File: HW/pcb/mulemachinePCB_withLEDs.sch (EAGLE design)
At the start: 29 parts, among them IC1 LD117AV50, IC2 MEGA8-P, J1 DCJ0202, Q1 16Mhz

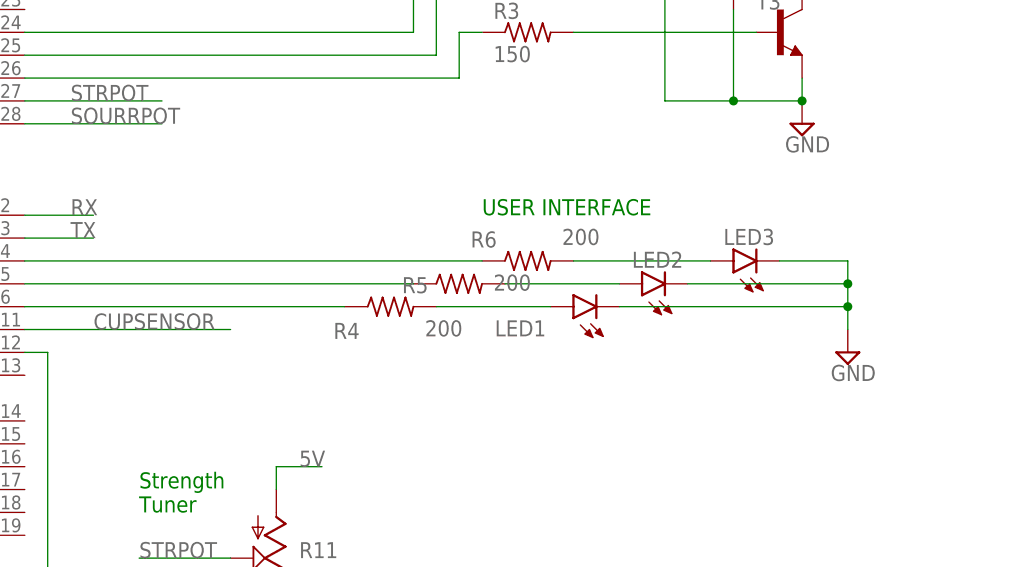
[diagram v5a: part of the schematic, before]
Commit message: preparing files for first prototype of version 1.0 of Mule Machine. Corrected Code to reflect Orange and Green LEDs being flipped on PCB and Code. Used PCB Version. Added some new design features to laser panel and PCB for version 1.1
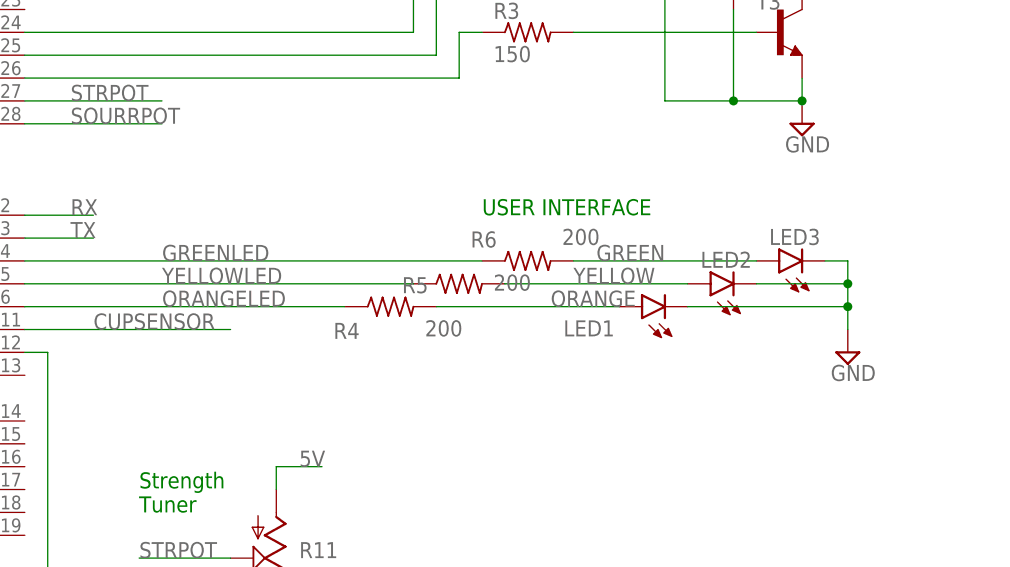
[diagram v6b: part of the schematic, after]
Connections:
- net N$2 renamed ORANGELED
- net N$25 renamed ORANGE
- net N$26 renamed YELLOW
- net N$27 renamed GREEN
- net N$3 renamed YELLOWLED
- net N$4 renamed GREENLED
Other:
- moved on the sheet: LED1, LED2, LED3
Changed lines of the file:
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@@
 <grid distance="0.1" unitdist="inch" unit="inch" style="lines" multiple="1" display="no" altdistance="0.01" altunitdist="inch" altunit="inch"/>
 <layers>
-<layer number="1" name="Top" color="4" fill="1" visible="yes" active="no"/>
-<layer number="16" name="Bottom" color="1" fill="1" visible="yes" active="no"/>
-<layer number="17" name="Pads" color="2" fill="1" visible="yes" active="no"/>
-<layer number="18" name="Vias" color="2" fill="1" visible="yes" active="no"/>
-<layer number="19" name="Unrouted" color="6" fill="1" visible="yes" active="no"/>
-<layer number="20" name="Dimension" color="24" fill="1" visible="yes" active="no"/>
-<layer number="21" name="tPlace" color="7" fill="1" visible="yes" active="no"/>
-<layer number="22" name="bPlace" color="7" fill="1" visible="yes" active="no"/>
-<layer number="23" name="tOrigins" color="15" fill="1" visible="yes" active="no"/>
-<layer number="24" name="bOrigins" color="15" fill="1" visible="yes" active="no"/>
-<layer number="25" name="tNames" color="7" fill="1" visible="yes" active="no"/>
-<layer number="26" name="bNames" color="7" fill="1" visible="yes" active="no"/>
-<layer number="27" name="tValues" color="7" fill="1" visible="yes" active="no"/>
-<layer number="28" name="bValues" color="7" fill="1" visible="yes" active="no"/>
+<layer number="1" name="Top" color="4" fill="1" visible="no" active="no"/>
+<layer number="16" name="Bottom" color="1" fill="1" visible="no" active="no"/>
+<layer number="17" name="Pads" color="2" fill="1" visible="no" active="no"/>
+<layer number="18" name="Vias" color="2" fill="1" visible="no" active="no"/>
+<layer number="19" name="Unrouted" color="6" fill="1" visible="no" active="no"/>
+<layer number="20" name="Dimension" color="24" fill="1" visible="no" active="no"/>
+<layer number="21" name="tPlace" color="7" fill="1" visible="no" active="no"/>
+<layer number="22" name="bPlace" color="7" fill="1" visible="no" active="no"/>
+<layer number="23" name="tOrigins" color="15" fill="1" visible="no" active="no"/>
+<layer number="24" name="bOrigins" color="15" fill="1" visible="no" active="no"/>
+<layer number="25" name="tNames" color="7" fill="1" visible="no" active="no"/>
+<layer number="26" name="bNames" color="7" fill="1" visible="no" active="no"/>
+<layer number="27" name="tValues" color="7" fill="1" visible="no" active="no"/>
+<layer number="28" name="bValues" color="7" fill="1" visible="no" active="no"/>
 <layer number="29" name="tStop" color="7" fill="3" visible="no" active="no"/>
 <layer number="30" name="bStop" color="7" fill="6" visible="no" active="no"/>
@@
 <layer number="35" name="tGlue" color="7" fill="4" visible="no" active="no"/>
 <layer number="36" name="bGlue" color="7" fill="5" visible="no" active="no"/>
-<layer number="37" name="tTest" color="7" fill="1" visible="yes" active="no"/>
-<layer number="38" name="bTest" color="7" fill="1" visible="yes" active="no"/>
+<layer number="37" name="tTest" color="7" fill="1" visible="no" active="no"/>
+<layer number="38" name="bTest" color="7" fill="1" visible="no" active="no"/>
 <layer number="39" name="tKeepout" color="4" fill="11" visible="no" active="no"/>
 <layer number="40" name="bKeepout" color="1" fill="11" visible="no" active="no"/>
@@
 <layer number="44" name="Drills" color="7" fill="1" visible="no" active="no"/>
 <layer number="45" name="Holes" color="7" fill="1" visible="no" active="no"/>
-<layer number="46" name="Milling" color="3" fill="1" visible="yes" active="no"/>
-<layer number="47" name="Measures" color="7" fill="1" visible="yes" active="no"/>
-<layer number="48" name="Document" color="7" fill="1" visible="yes" active="no"/>
-<layer number="49" name="Reference" color="7" fill="1" visible="yes" active="no"/>
-<layer number="51" name="tDocu" color="7" fill="1" visible="yes" active="no"/>
-<layer number="52" name="bDocu" color="7" fill="1" visible="yes" active="no"/>
+<layer number="46" name="Milling" color="3" fill="1" visible="no" active="no"/>
+<layer number="47" name="Measures" color="7" fill="1" visible="no" active="no"/>
+<layer number="48" name="Document" color="7" fill="1" visible="no" active="no"/>
+<layer number="49" name="Reference" color="7" fill="1" visible="no" active="no"/>
+<layer number="51" name="tDocu" color="7" fill="1" visible="no" active="no"/>
+<layer number="52" name="bDocu" color="7" fill="1" visible="no" active="no"/>
 <layer number="88" name="SimResults" color="9" fill="1" visible="yes" active="yes"/>
 <layer number="89" name="SimProbes" color="9" fill="1" visible="yes" active="yes"/>
@@
 <attribute name="VALUE" x="-1.905" y="73.025" size="1.778" layer="96"/>
 </instance>
-<instance part="LED1" gate="G$1" x="134.62" y="50.8" smashed="yes" rot="R90">
-<attribute name="NAME" x="131.572" y="49.276" size="1.778" layer="95" rot="R180"/>
-<attribute name="VALUE" x="139.192" y="56.515" size="1.778" layer="96" rot="R180"/>
-</instance>
-<instance part="LED2" gate="G$1" x="142.24" y="53.34" smashed="yes" rot="R90">
-<attribute name="NAME" x="146.812" y="56.896" size="1.778" layer="95" rot="R180"/>
-<attribute name="VALUE" x="146.812" y="59.055" size="1.778" layer="96" rot="R180"/>
-</instance>
-<instance part="LED3" gate="G$1" x="152.4" y="55.88" smashed="yes" rot="R90">
-<attribute name="NAME" x="156.972" y="59.436" size="1.778" layer="95" rot="R180"/>
-<attribute name="VALUE" x="156.972" y="61.595" size="1.778" layer="96" rot="R180"/>
+<instance part="LED1" gate="G$1" x="142.24" y="50.8" smashed="yes" rot="R90">
+<attribute name="NAME" x="139.192" y="49.276" size="1.778" layer="95" rot="R180"/>
+<attribute name="VALUE" x="146.812" y="56.515" size="1.778" layer="96" rot="R180"/>
+</instance>
+<instance part="LED2" gate="G$1" x="149.86" y="53.34" smashed="yes" rot="R90">
+<attribute name="NAME" x="154.432" y="56.896" size="1.778" layer="95" rot="R180"/>
+<attribute name="VALUE" x="154.432" y="59.055" size="1.778" layer="96" rot="R180"/>
+</instance>
+<instance part="LED3" gate="G$1" x="157.48" y="55.88" smashed="yes" rot="R90">
+<attribute name="NAME" x="162.052" y="59.436" size="1.778" layer="95" rot="R180"/>
+<attribute name="VALUE" x="162.052" y="61.595" size="1.778" layer="96" rot="R180"/>
 </instance>
 <instance part="SUPPLY2" gate="GND" x="165.1" y="45.72" smashed="yes">
@@
 <segment>
 <pinref part="LED3" gate="G$1" pin="C"/>
-<wire x1="157.48" y1="55.88" x2="165.1" y2="55.88" width="0.1524" layer="91"/>
+<wire x1="162.56" y1="55.88" x2="165.1" y2="55.88" width="0.1524" layer="91"/>
 <pinref part="SUPPLY2" gate="GND" pin="GND"/>
 <wire x1="165.1" y1="55.88" x2="165.1" y2="53.34" width="0.1524" layer="91"/>
@@
 <wire x1="165.1" y1="53.34" x2="165.1" y2="50.8" width="0.1524" layer="91"/>
 <wire x1="165.1" y1="50.8" x2="165.1" y2="48.26" width="0.1524" layer="91"/>
-<wire x1="147.32" y1="53.34" x2="165.1" y2="53.34" width="0.1524" layer="91"/>
+<wire x1="154.94" y1="53.34" x2="165.1" y2="53.34" width="0.1524" layer="91"/>
 <junction x="165.1" y="53.34"/>
 <pinref part="LED1" gate="G$1" pin="C"/>
-<wire x1="139.7" y1="50.8" x2="165.1" y2="50.8" width="0.1524" layer="91"/>
+<wire x1="147.32" y1="50.8" x2="165.1" y2="50.8" width="0.1524" layer="91"/>
 <junction x="165.1" y="50.8"/>
 </segment>
@@
 </segment>
 </net>
-<net name="N$2" class="0">
+<net name="ORANGELED" class="0">
 <segment>
 <wire x1="73.66" y1="50.8" x2="109.22" y2="50.8" width="0.1524" layer="91"/>
 <pinref part="R4" gate="G$1" pin="1"/>
 <pinref part="IC2" gate="G$1" pin="PD4(XCK/T0)"/>
-</segment>
-</net>
-<net name="N$4" class="0">
+<label x="88.9" y="50.8" size="1.778" layer="95"/>
+</segment>
+</net>
+<net name="GREENLED" class="0">
 <segment>
 <wire x1="73.66" y1="55.88" x2="124.46" y2="55.88" width="0.1524" layer="91"/>
 <pinref part="R6" gate="G$1" pin="1"/>
 <pinref part="IC2" gate="G$1" pin="PD2(INT0)"/>
+<label x="88.9" y="55.88" size="1.778" layer="95"/>
 </segment>
 </net>
@@
 </segment>
 </net>
-<net name="N$3" class="0">
+<net name="YELLOWLED" class="0">
 <segment>
 <pinref part="IC2" gate="G$1" pin="PD3(INT1)"/>
 <wire x1="73.66" y1="53.34" x2="116.84" y2="53.34" width="0.1524" layer="91"/>
 <pinref part="R5" gate="G$1" pin="1"/>
-</segment>
-</net>
-<net name="N$25" class="0">
+<label x="88.9" y="53.34" size="1.778" layer="95"/>
+</segment>
+</net>
+<net name="ORANGE" class="0">
 <segment>
 <pinref part="LED1" gate="G$1" pin="A"/>
 <pinref part="R4" gate="G$1" pin="2"/>
-<wire x1="132.08" y1="50.8" x2="119.38" y2="50.8" width="0.1524" layer="91"/>
-</segment>
-</net>
-<net name="N$26" class="0">
+<wire x1="139.7" y1="50.8" x2="119.38" y2="50.8" width="0.1524" layer="91"/>
+<label x="132.08" y="50.8" size="1.778" layer="95"/>
+</segment>
+</net>
+<net name="YELLOW" class="0">
 <segment>
 <pinref part="LED2" gate="G$1" pin="A"/>
 <pinref part="R5" gate="G$1" pin="2"/>
-<wire x1="139.7" y1="53.34" x2="127" y2="53.34" width="0.1524" layer="91"/>
-</segment>
-</net>
-<net name="N$27" class="0">
+<wire x1="147.32" y1="53.34" x2="127" y2="53.34" width="0.1524" layer="91"/>
+<label x="134.62" y="53.34" size="1.778" layer="95"/>
+</segment>
+</net>
+<net name="GREEN" class="0">
 <segment>
 <pinref part="R6" gate="G$1" pin="2"/>
 <pinref part="LED3" gate="G$1" pin="A"/>
-<wire x1="134.62" y1="55.88" x2="149.86" y2="55.88" width="0.1524" layer="91"/>
-</segment>
-</net>
+<wire x1="134.62" y1="55.88" x2="154.94" y2="55.88" width="0.1524" layer="91"/>
+<label x="137.16" y="55.88" size="1.778" layer="95"/>
+</segment>
+</net>

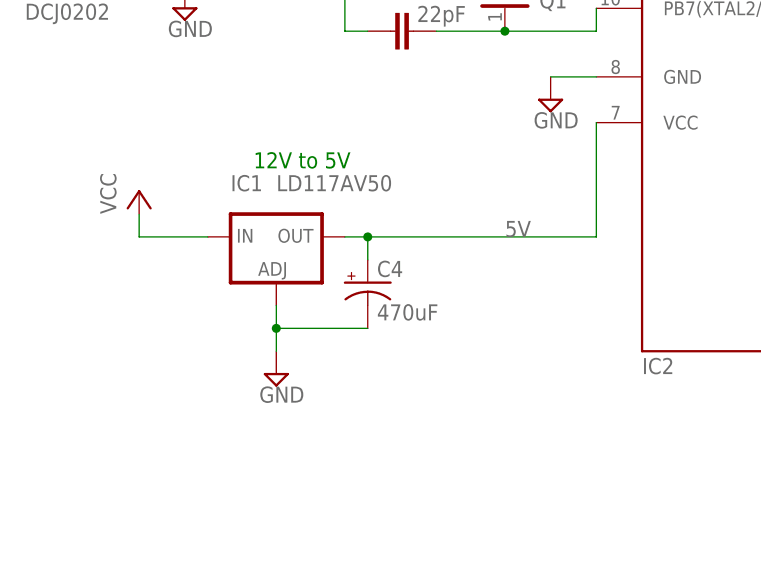
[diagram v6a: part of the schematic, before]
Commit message: fixed #13 with additional 100uF cap on 12V power line and 0.1uF cap on 5v line in parallel with 470uF cap. This smooths the 12V line and the 5V line for more powerful motors. needs more duration of bootup time to get caps charged, but can run Mixing Mode with full strength and sourness settings for > 5 minutes. Tested on V1.0 PCB. Implemented caps into V1.1 PCB and re-autorouted.
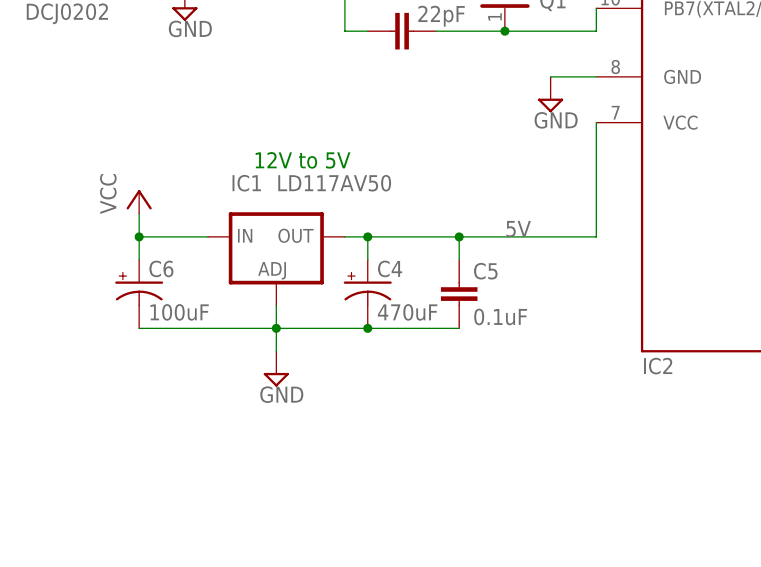
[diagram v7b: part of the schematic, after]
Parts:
- added C5: 0.1uF, capacitor-wima:C2,5-3
- added C6: 100uF, rcl:CPOL-USE2.5-6
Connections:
- net 5V: now also C5.1
- net GND: now also C5.2, C6.-
- net VCC: now also C6.+
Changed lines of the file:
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@@
 <part name="T2" library="transistor-neu-to92" library_urn="urn:adsk.eagle:library:397" deviceset="*-NPN-" device="TO92-EBC" package3d_urn="urn:adsk.eagle:package:28763/2" technology="2N4401"/>
 <part name="T3" library="transistor-neu-to92" library_urn="urn:adsk.eagle:library:397" deviceset="*-NPN-" device="TO92-EBC" package3d_urn="urn:adsk.eagle:package:28763/2" technology="2N4401"/>
+<part name="C5" library="capacitor-wima" library_urn="urn:adsk.eagle:library:116" deviceset="C" device="2,5-3" package3d_urn="urn:adsk.eagle:package:5436/1" value="0.1uF"/>
+<part name="C6" library="rcl" library_urn="urn:adsk.eagle:library:334" deviceset="CPOL-US" device="E2.5-6" package3d_urn="urn:adsk.eagle:package:23349/1" value="100uF"/>
 </parts>
 <sheets>
@@
 <attribute name="VALUE" x="147.32" y="86.36" size="1.778" layer="96"/>
 </instance>
+<instance part="C5" gate="G$1" x="10.16" y="30.48" smashed="yes">
+<attribute name="NAME" x="11.684" y="30.861" size="1.778" layer="95"/>
+<attribute name="VALUE" x="11.684" y="25.781" size="1.778" layer="96"/>
+</instance>
+<instance part="C6" gate="G$1" x="-25.4" y="30.48" smashed="yes">
+<attribute name="NAME" x="-24.384" y="31.115" size="1.778" layer="95"/>
+<attribute name="VALUE" x="-24.384" y="26.289" size="1.778" layer="96"/>
+</instance>
 </instances>
 <busses>
@@
 <wire x1="-25.4" y1="38.1" x2="-25.4" y2="35.56" width="0.1524" layer="91"/>
 <wire x1="-25.4" y1="35.56" x2="-17.78" y2="35.56" width="0.1524" layer="91"/>
+<pinref part="C6" gate="G$1" pin="+"/>
+<wire x1="-25.4" y1="33.02" x2="-25.4" y2="35.56" width="0.1524" layer="91"/>
+<junction x="-25.4" y="35.56"/>
 </segment>
 <segment>
@@
 <junction x="-10.16" y="25.4"/>
 <pinref part="C4" gate="G$1" pin="-"/>
+<pinref part="C5" gate="G$1" pin="2"/>
+<wire x1="0" y1="25.4" x2="10.16" y2="25.4" width="0.1524" layer="91"/>
+<junction x="0" y="25.4"/>
+<pinref part="C6" gate="G$1" pin="-"/>
+<wire x1="-25.4" y1="25.4" x2="-10.16" y2="25.4" width="0.1524" layer="91"/>
 </segment>
 <segment>
@@
 <pinref part="IC1" gate="G$1" pin="OUT"/>
 <wire x1="-2.54" y1="35.56" x2="0" y2="35.56" width="0.1524" layer="91"/>
-<wire x1="0" y1="35.56" x2="25.4" y2="35.56" width="0.1524" layer="91"/>
+<wire x1="0" y1="35.56" x2="10.16" y2="35.56" width="0.1524" layer="91"/>
+<wire x1="10.16" y1="35.56" x2="25.4" y2="35.56" width="0.1524" layer="91"/>
 <wire x1="0" y1="33.02" x2="0" y2="35.56" width="0.1524" layer="91"/>
 <junction x="0" y="35.56"/>
@@
 <label x="15.24" y="35.56" size="1.778" layer="95"/>
 <pinref part="C4" gate="G$1" pin="+"/>
-</segment>
-<segment>
+<pinref part="C5" gate="G$1" pin="1"/>
+<wire x1="10.16" y1="33.02" x2="10.16" y2="35.56" width="0.1524" layer="91"/>
+<junction x="10.16" y="35.56"/>
+</segment>
+<segment>
